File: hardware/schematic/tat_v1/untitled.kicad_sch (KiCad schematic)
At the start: 16 parts, among them J2 USB_C_Receptacle_USB2.0_14P, J3 Conn_01x02_Pin, U5 BQ25185, U6 TPS631000DRLR

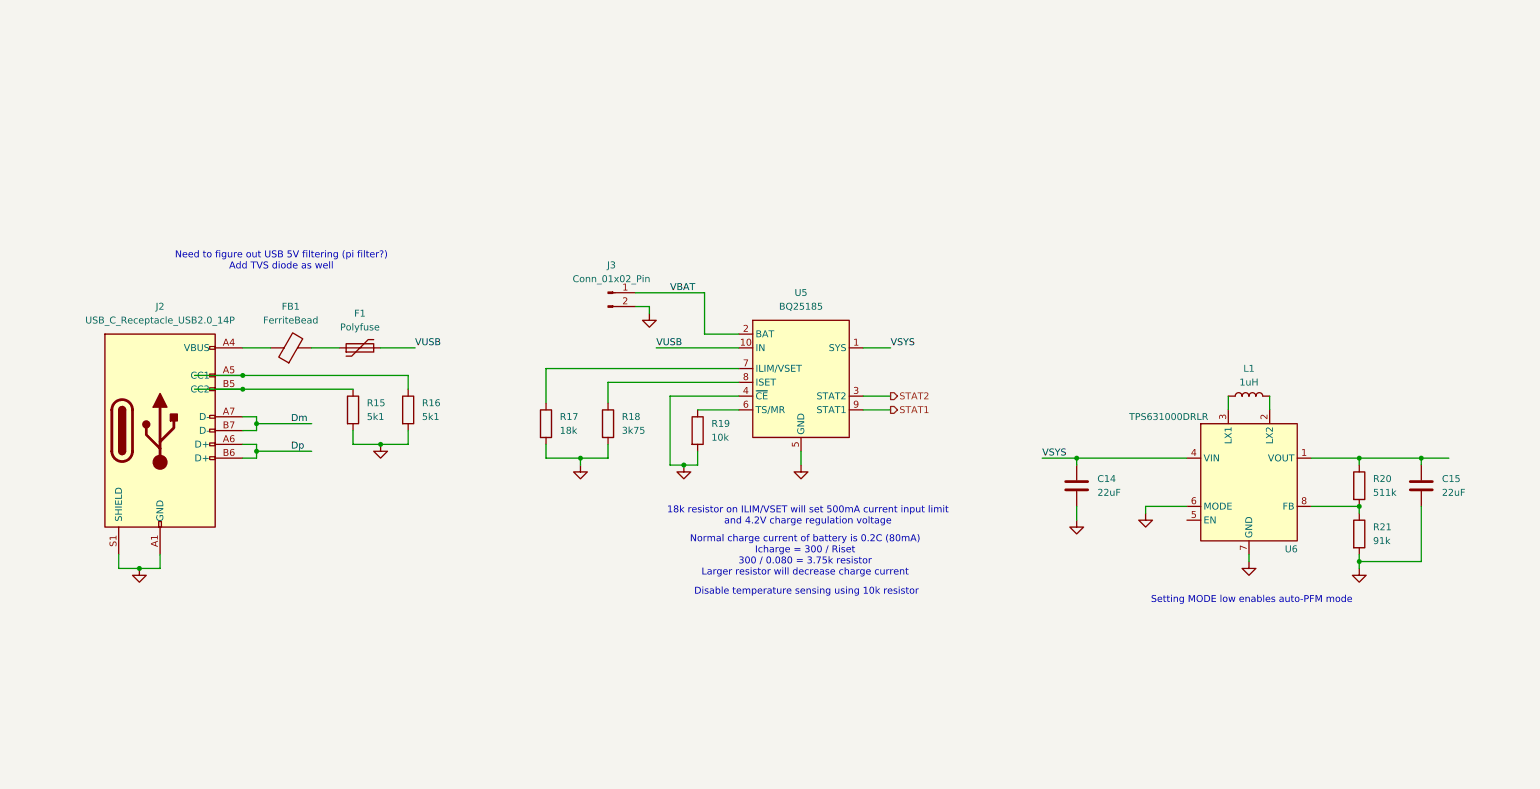
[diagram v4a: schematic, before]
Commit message: Completed basic implementation of USB and battery charger schematic. Need to finish buck-boost part
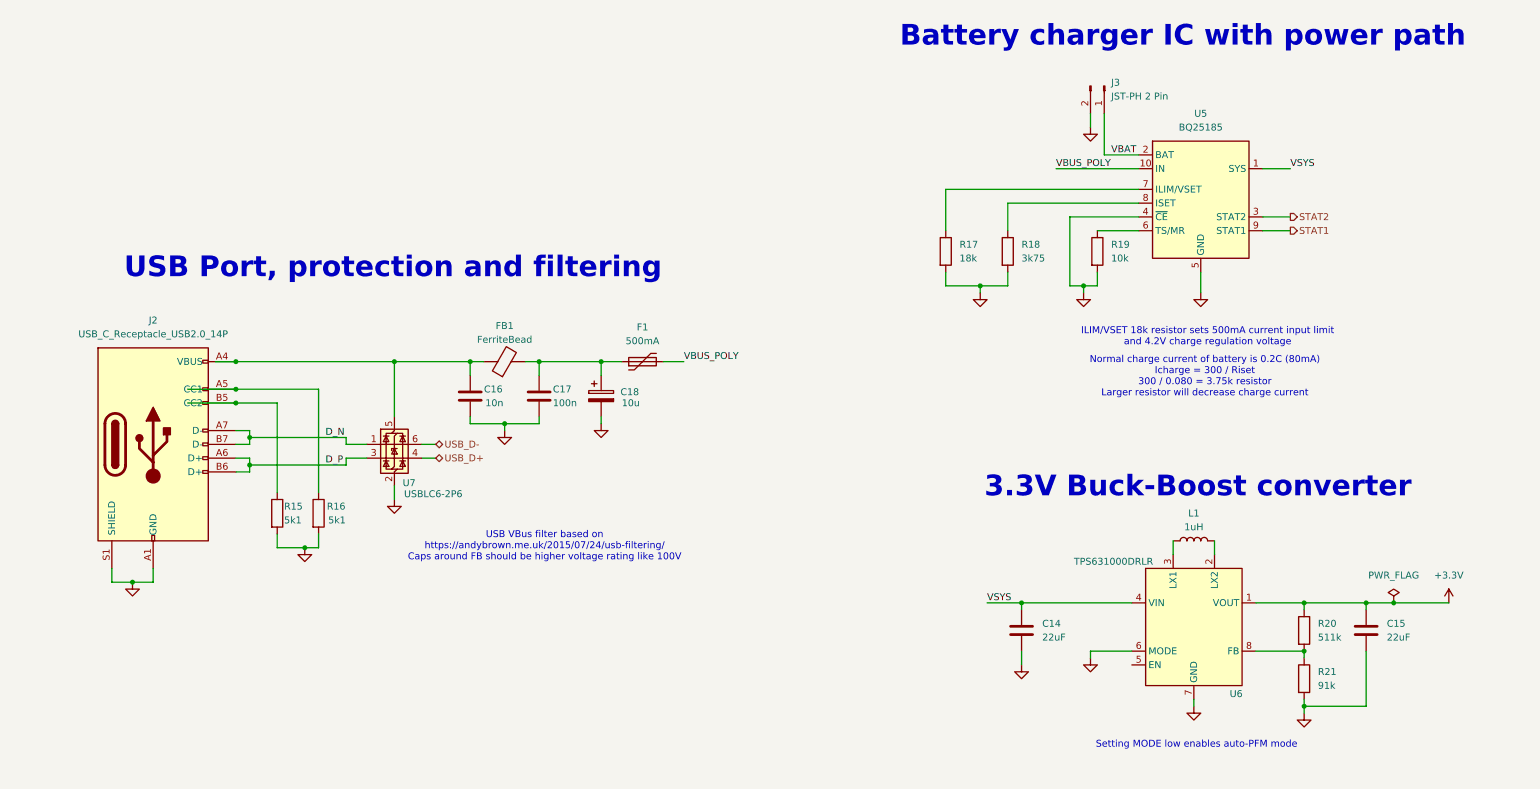
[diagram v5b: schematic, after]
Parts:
- added C16: 10n, symbol Device:C
- added C17: 100n, symbol Device:C
- added C18: 10u, symbol Device:C_Polarized
- added U7: USBLC6-2P6, Package_TO_SOT_SMD:SOT-666, symbol Power_Protection:USBLC6-2P6
- F1: value Polyfuse -> 500mA
- J3: value Conn_01x02_Pin -> JST-PH 2 Pin
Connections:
- net GND: now also C16.2, C17.2, C18.2, U7.2 (GND)
- net +3.3V: now reaches C15.1, R20.1, U6.1 (VOUT)
- net at FB1.1, J2.A4 (VBUS), J2.A9 (VBUS)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: now also C16.1, U7.5 (VBUS)
- net at F1.1, FB1.2: now also C17.1, C18.1
- net Dm renamed D_N
- net D_N: now also U7.1 (I/O1)
- net Dp renamed D_P
- net D_P: now also U7.3 (I/O2)
- net VUSB renamed VBUS_POLY
- new net USB_D+: U7.4 (I/O2)
- new net USB_D-: U7.6 (I/O1)
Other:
- note added: "3.3V Buck-Boost converter"
- note added: "Battery charger IC with power path"
- note added: "ILIM/VSET 18k resistor sets 500mA current input limit and 4.2V charge regulation voltage"
- note added: "USB Port, protection and filtering"
- note added: "USB VBus filter based on https://andybrown.me.uk/2015/07/24/usb-filtering/ Caps around FB should be higher voltage rating like 100V"
- note removed: "18k resistor on ILIM/VSET will set 500mA current input limit and 4.2V charge regulation voltage"
- note removed: "Disable temperature sensing using 10k resistor"
- note removed: "Need to figure out USB 5V filtering (pi filter?) Add TVS diode as well"
- moved on the sheet: C14, C15, F1, J2, J3, L1, R15, R16, R17, R18, R19, R20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

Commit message: Basic circuit is complete, needs double checking
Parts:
- added D4: BLUE, symbol Device:LED
- added R22: 2k, symbol Device:R
- added R25: 33k, symbol Device:R
- added R26: 82k, symbol Device:R
- added SW6: SW_SPDT, symbol Switch:SW_SPDT
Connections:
- net GND: now also R22.2, R26.2, SW6.1 (A)
- net VSYS: now also SW6.3 (C)
- net at U6.5 (EN): now also SW6.2 (B)
- net VBUS_POLY renamed VUSB
- net VUSB: now also D4.2 (A), R25.1
- new net: D4.1 (K), R22.1
- new net USB Sense: R25.2, R26.1
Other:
- note added: "Imax = 1mA"
- note added: "Setting MODE low enables auto-PFM mode Values from reference in datasheet"
- note removed: "Setting MODE low enables auto-PFM mode"
- moved on the sheet: C14, R17

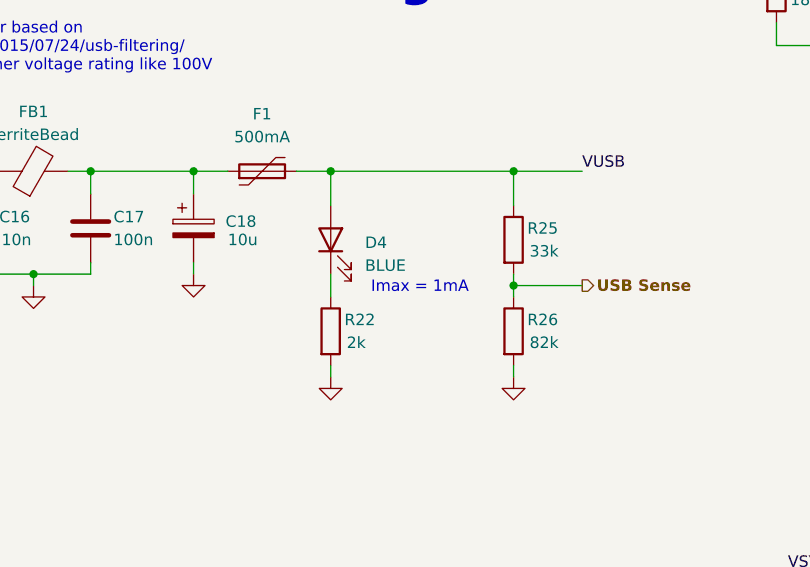
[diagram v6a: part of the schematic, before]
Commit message: Need to implement checking battery charge tracking
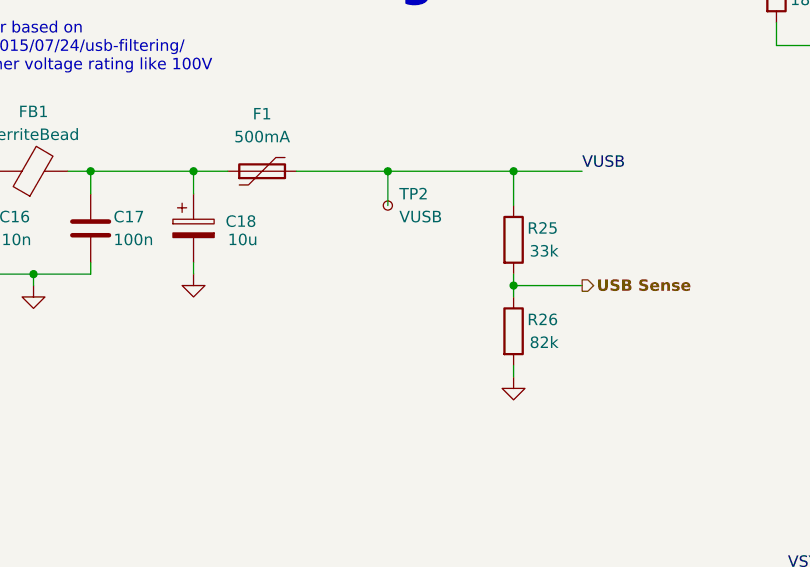
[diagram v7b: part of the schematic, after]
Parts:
- removed D4: BLUE, symbol Device:LED
- removed R22: 2k, symbol Device:R
- added TP2: VUSB, symbol Connector:TestPoint_Small
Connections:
- net VUSB: now also TP2.1
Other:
- note removed: "Imax = 1mA"
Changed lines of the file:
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@@
-		)
-	)
-	(text "Imax = 1mA\n"
-		(exclude_from_sim no)
-		(at 141.986 96.774 0)
-		(effects
-			(font
-				(size 1.27 1.27)
-			)
 		)
 	)
@@
 	)
 	(junction
+		(at 138.43 83.82)
+		(diameter 0)
+		(color 0 0 0 0)
+	)
+	(junction
 		(at 257.81 128.27)
 		(diameter 0)
@@
 	)
 	(junction
-		(at 132.08 83.82)
-		(diameter 0)
-		(color 0 0 0 0)
-	)
-	(junction
 		(at 205.74 69.85)
 		(diameter 0)
@@
 	(wire
 		(pts
-			(xy 132.08 83.82) (xy 132.08 87.63)
-		)
-		(stroke
-			(width 0)
-			(type default)
-		)
-	)
-	(wire
-		(pts
 			(xy 69.85 97.79) (xy 69.85 99.06)
 		)
@@
 	(wire
 		(pts
-			(xy 132.08 95.25) (xy 132.08 97.79)
-		)
-		(stroke
-			(width 0)
-			(type default)
-		)
-	)
-	(wire
-		(pts
 			(xy 181.61 69.85) (xy 186.69 69.85)
 		)
@@
 	(wire
 		(pts
-			(xy 132.08 105.41) (xy 132.08 106.68)
-		)
-		(stroke
-			(width 0)
-			(type default)
-		)
-	)
-	(wire
-		(pts
 			(xy 191.77 54.61) (xy 215.9 54.61)
 		)
@@
 	(wire
 		(pts
-			(xy 128.27 83.82) (xy 132.08 83.82)
+			(xy 128.27 83.82) (xy 138.43 83.82)
 		)
 		(stroke
@@
 	(wire
 		(pts
+			(xy 138.43 83.82) (xy 138.43 87.63)
+		)
+		(stroke
+			(width 0)
+			(type default)
+		)
+	)
+	(wire
+		(pts
 			(xy 152.4 96.52) (xy 152.4 97.79)
 		)
@@
 	(wire
 		(pts
+			(xy 138.43 83.82) (xy 152.4 83.82)
+		)
+		(stroke
+			(width 0)
+			(type default)
+		)
+	)
+	(wire
+		(pts
 			(xy 209.55 48.26) (xy 215.9 48.26)
 		)
@@
 		(pts
 			(xy 152.4 96.52) (xy 160.02 96.52)
-		)
-		(stroke
-			(width 0)
-			(type default)
-		)
-	)
-	(wire
-		(pts
-			(xy 132.08 83.82) (xy 152.4 83.82)
 		)
 		(stroke
@@
 	)
 	(symbol
-		(lib_id "Device:LED")
-		(at 132.08 91.44 90)
-		(unit 1)
-		(exclude_from_sim no)
-		(in_bom yes)
-		(on_board yes)
-		(dnp no)
-		(fields_autoplaced yes)
-		(property "Reference" "D4"
-			(at 135.89 91.7574 90)
-			(effects
-				(font
-					(size 1.27 1.27)
-				)
-				(justify right)
-			)
-		)
-		(property "Value" "BLUE"
-			(at 135.89 94.2974 90)
-			(effects
-				(font
-					(size 1.27 1.27)
-				)
-				(justify right)
-			)
-		)
-		(property "Footprint" ""
-			(at 132.08 91.44 0)
-			(effects
-				(font
-					(size 1.27 1.27)
-				)
-				(hide yes)
-			)
-		)
-		(property "Datasheet" "~"
-			(at 132.08 91.44 0)
-			(effects
-				(font
-					(size 1.27 1.27)
-				)
-				(hide yes)
-			)
-		)
-		(property "Description" "Light emitting diode"
-			(at 132.08 91.44 0)
-			(effects
-				(font
-					(size 1.27 1.27)
-				)
-				(hide yes)
-			)
-		)
-		(property "Sim.Pins" "1=K 2=A"
-			(at 132.08 91.44 0)
-			(effects
-				(font
-					(size 1.27 1.27)
-				)
-				(hide yes)
-			)
-		)
-		(pin "2"
-		)
-		(pin "1"
-		)
-		(instances
-			(project ""
-				(path "/b6d2ddf1-6792-45dd-afc9-29fd74d587ec/5056535a-bc75-42d4-a05e-c6bbb85e2678"
-					(reference "D4")
-					(unit 1)
-				)
-			)
-		)
-	)
-	(symbol
 		(lib_id "power:GND")
 		(at 116.84 95.25 0)
@@
 				(path "/b6d2ddf1-6792-45dd-afc9-29fd74d587ec/5056535a-bc75-42d4-a05e-c6bbb85e2678"
 					(reference "#PWR042")
-					(unit 1)
-				)
-			)
-		)
-	)
-	(symbol
-		(lib_id "Device:R")
-		(at 132.08 101.6 0)
-		(unit 1)
-		(exclude_from_sim no)
-		(in_bom yes)
-		(on_board yes)
-		(dnp no)
-		(property "Reference" "R22"
-			(at 133.604 100.33 0)
-			(effects
-				(font
-					(size 1.27 1.27)
-				)
-				(justify left)
-			)
-		)
-		(property "Value" "2k"
-			(at 133.858 102.87 0)
-			(effects
-				(font
-					(size 1.27 1.27)
-				)
-				(justify left)
-			)
-		)
-		(property "Footprint" ""
-			(at 130.302 101.6 90)
-			(effects
-				(font
-					(size 1.27 1.27)
-				)
-				(hide yes)
-			)
-		)
-		(property "Datasheet" "~"
-			(at 132.08 101.6 0)
-			(effects
-				(font
-					(size 1.27 1.27)
-				)
-				(hide yes)
-			)
-		)
-		(property "Description" "Resistor"
-			(at 132.08 101.6 0)
-			(effects
-				(font
-					(size 1.27 1.27)
-				)
-				(hide yes)
-			)
-		)
-		(pin "1"
-		)
-		(pin "2"
-		)
-		(instances
-			(project "tat_v1"
-				(path "/b6d2ddf1-6792-45dd-afc9-29fd74d587ec/5056535a-bc75-42d4-a05e-c6bbb85e2678"
-					(reference "R22")
 					(unit 1)
 				)
@@
 	)
 	(symbol
-		(lib_id "power:GND")
-		(at 132.08 106.68 0)
-		(unit 1)
-		(exclude_from_sim no)
-		(in_bom yes)
-		(on_board yes)
-		(dnp no)
-		(fields_autoplaced yes)
-		(property "Reference" "#PWR047"
-			(at 132.08 113.03 0)
-			(effects
-				(font
-					(size 1.27 1.27)
-				)
-				(hide yes)
-			)
-		)
-		(property "Value" "GND"
-			(at 132.08 111.76 0)
-			(effects
-				(font
-					(size 1.27 1.27)
-				)
-				(hide yes)
-			)
-		)
-		(property "Footprint" ""
-			(at 132.08 106.68 0)
-			(effects
-				(font
-					(size 1.27 1.27)
-				)
-				(hide yes)
-			)
-		)
-		(property "Datasheet" ""
-			(at 132.08 106.68 0)
-			(effects
-				(font
-					(size 1.27 1.27)
-				)
-				(hide yes)
-			)
-		)
-		(property "Description" "Power symbol creates a global label with name \"GND\" , ground"
-			(at 132.08 106.68 0)
-			(effects
-				(font
-					(size 1.27 1.27)
-				)
-				(hide yes)
-			)
-		)
-		(pin "1"
-		)
-		(instances
-			(project "tat_v1"
-				(path "/b6d2ddf1-6792-45dd-afc9-29fd74d587ec/5056535a-bc75-42d4-a05e-c6bbb85e2678"
-					(reference "#PWR047")
-					(unit 1)
-				)
-			)
-		)
-	)
-	(symbol
 		(lib_id "power:PWR_FLAG")
 		(at 262.89 128.27 0)
@@
 					(unit 1)
 				)
+			)
+		)
+	)
+	(symbol
+		(lib_id "Connector:TestPoint_Small")
+		(at 138.43 87.63 0)
+		(unit 1)
+		(exclude_from_sim no)
+		(in_bom yes)
+		(on_board yes)
+		(dnp no)
+		(fields_autoplaced yes)
+		(property "Reference" "TP2"
+			(at 139.7 86.3599 0)
+			(effects
+				(font
+					(size 1.27 1.27)
+				)
+				(justify left)
+			)
+		)
+		(property "Value" "VUSB"
+			(at 139.7 88.8999 0)
+			(effects
+				(font
+					(size 1.27 1.27)
+				)
+				(justify left)
+			)
+		)
+		(property "Footprint" ""
+			(at 143.51 87.63 0)
+			(effects
+				(font
+					(size 1.27 1.27)
+				)
+				(hide yes)
+			)
+		)
+		(property "Datasheet" "~"
+			(at 143.51 87.63 0)
+			(effects
+				(font
+					(size 1.27 1.27)
+				)
+				(hide yes)
+			)
+		)
+		(property "Description" "test point"
+			(at 138.43 87.63 0)
+			(effects
+				(font
+					(size 1.27 1.27)
+				)
+				(hide yes)
+			)
+		)
+		(pin "1"
+		)
+		(instances
+			(project ""
+				(path "/b6d2ddf1-6792-45dd-afc9-29fd74d587ec/5056535a-bc75-42d4-a05e-c6bbb85e2678"
+					(reference "TP2")
+					(unit 1)
+				)

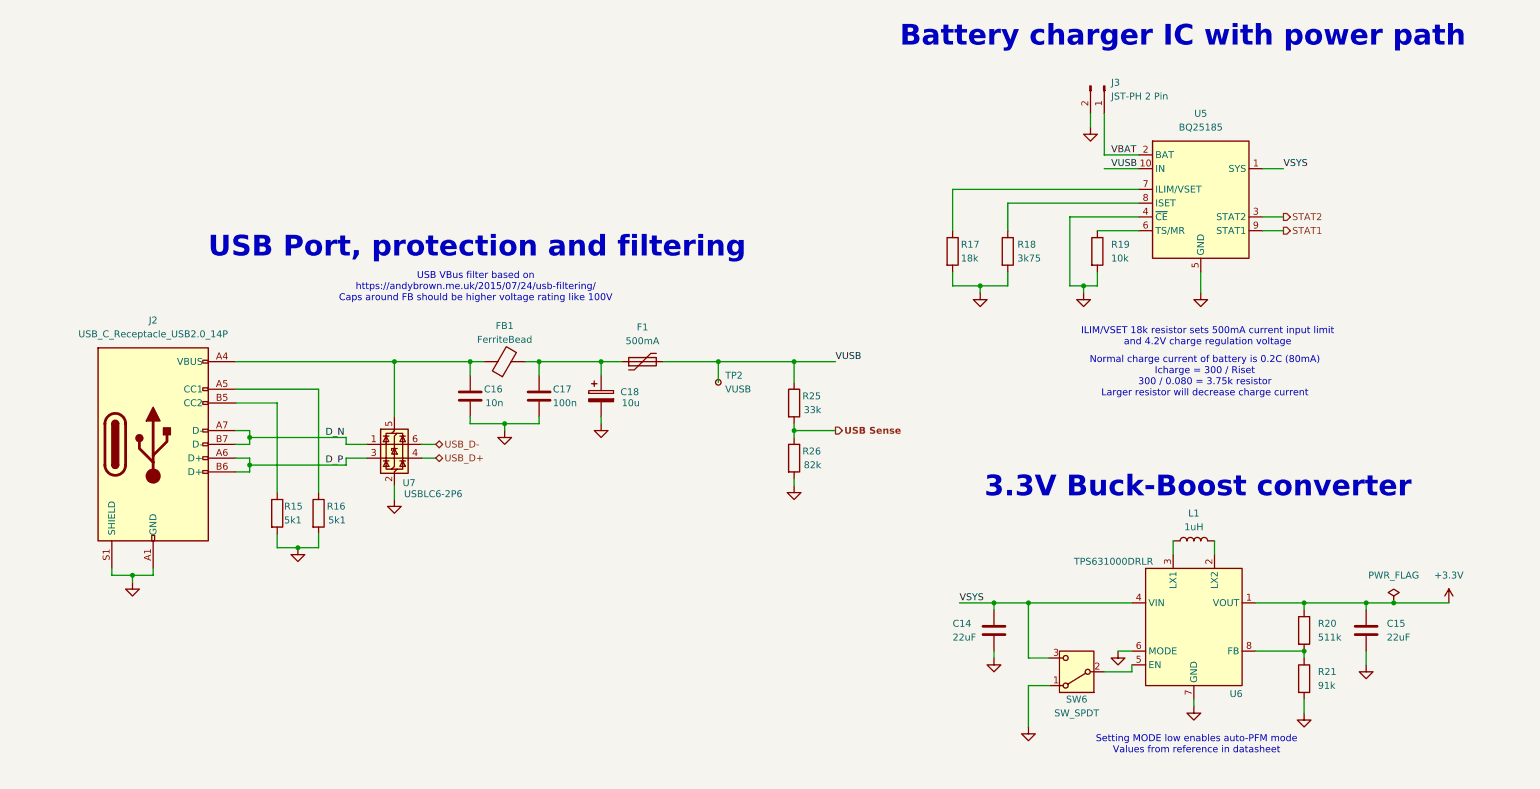
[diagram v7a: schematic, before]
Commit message: Added measuring battery voltage using the ADC. Basic schematic is complete, needs checking and refinement
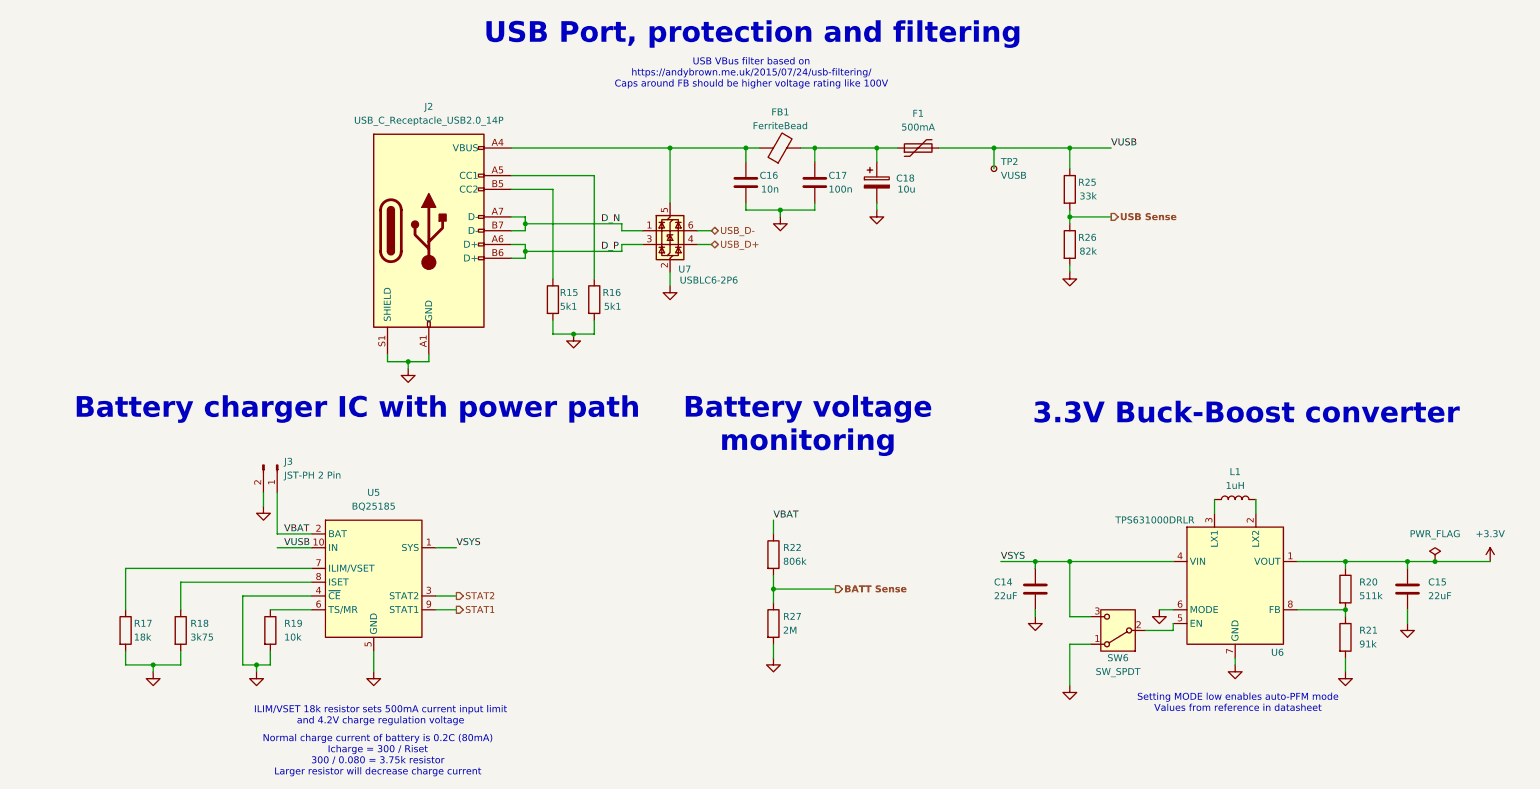
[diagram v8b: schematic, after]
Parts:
- added R22: 806k, symbol Device:R
- added R27: 2M, symbol Device:R
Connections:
- net GND: now also R27.2
- net VBAT: now also R22.1
- new net BATT Sense: R22.2, R27.1
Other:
- note added: "Battery voltage monitoring"
- moved on the sheet: C14, C15, C16, C17, C18, F1, FB1, J2, J3, L1, R15, R16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
